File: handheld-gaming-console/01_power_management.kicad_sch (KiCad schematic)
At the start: 34 parts, among them J1 USB_C_Receptacle_USB2.0_16P, J2 BATT_3V7_JST, U1 BQ24075RGT, U2 TPS61088, U3 MAX17048

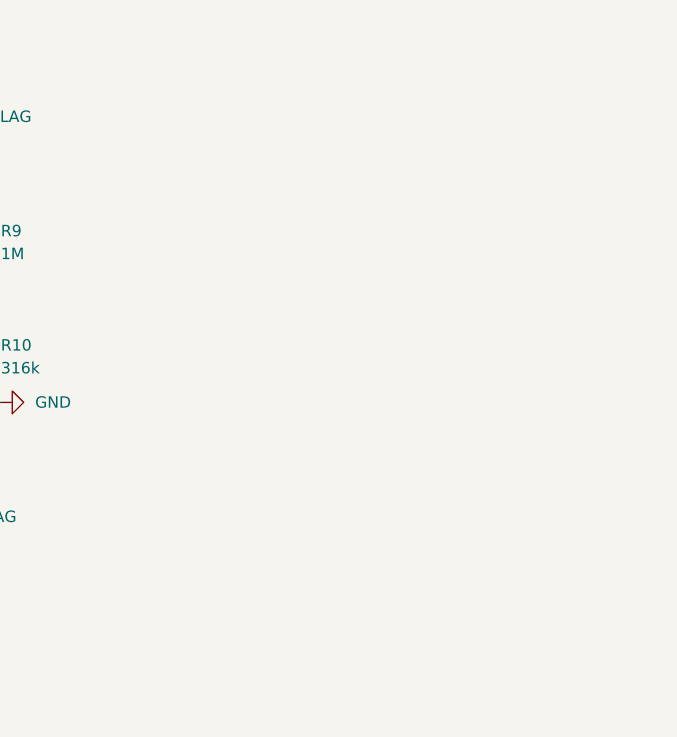
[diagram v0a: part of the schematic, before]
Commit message: feat(power): implement sequenced 3V3_PERIPH buck regulator for peripheral load safety
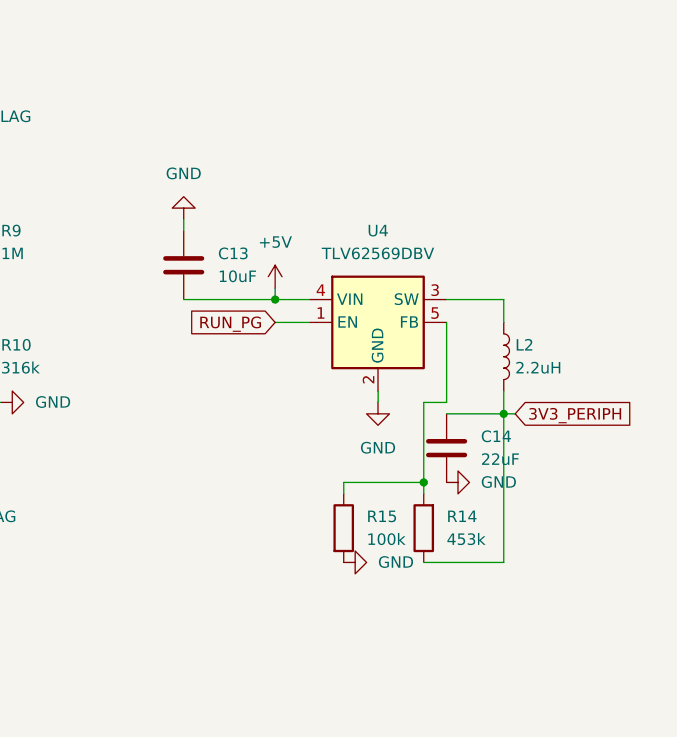
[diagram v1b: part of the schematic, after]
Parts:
- added C13: 10uF, symbol Device:C
- added C14: 22uF, symbol Device:C
- added L2: 2.2uH, Inductor_SMD:L_0805_2012Metric, symbol Device:L
- added R14: 453k, symbol Device:R
- added R15: 100k, symbol Device:R
- added U4: TLV62569DBV, Package_TO_SOT_SMD:SOT-23-5, symbol Regulator_Switching:TLV62569DBV
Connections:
- net +5V: now also C13.2, U4.4 (VIN)
- net GND: now also C13.1, C14.2, R15.2, U4.2 (GND)
- new net: L2.1, U4.3 (SW)
- new net: R14.2, R15.1, U4.5 (FB)
- new net 3V3_PERIPH: C14.1, L2.2, R14.1
- new net RUN_PG: U4.1 (EN)

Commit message: feat(usb): implement TS3USB221A high-speed mux, recovery switch, and otg role switching
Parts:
- added C15: 22uF, symbol Device:C
- added C16: 0.1uF, symbol Device:C
- added R16: 39k, symbol Device:R
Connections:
- net +5V: now also C15.2
- net GND: now also C15.1, C16.1, R16.1; no longer U1.14 (TMR)
- net VBAT: now also C16.2
- new net: R16.2, U1.14 (TMR)
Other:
- moved on the sheet: C8

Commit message: fix(core): correct J3 ground matrix, fix UART pins, add OTG_ID pull-up, and reduce BQ24075 input capacitance per design audit
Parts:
- C1: value 10uF -> 4.7uF
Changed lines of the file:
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@@
 			)
 		)
-		(property "Value" "10uF"
+		(property "Value" "4.7uF"
 			(at 111.76 86.3599 0)
 			(show_name no)

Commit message: feat(core): implement Rockchip-compliant MicroSD load switch, impedance damping, and ESD protection
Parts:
- C12: value 1uF -> 22uF
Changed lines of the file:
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@@
 			)
 		)
-		(property "Value" "1uF"
+		(property "Value" "22uF"
 			(at 175.26 22.86 90)
 			(show_name no)
